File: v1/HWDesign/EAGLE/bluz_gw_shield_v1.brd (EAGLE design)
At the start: 66 x 43.2 mm, 20 parts, among them Q1 FC-12M, U2 MDBT40SMD, U3 SST25VF040B-S2, U4 SPARK_CORE

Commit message: add reset button
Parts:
- added RESET: (no value), Spark:TACTILE_SWITCH_SMD
- moved C1 1.27 mm to (22.8, 40.9)
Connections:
- removed net SWDIO: SWD.2, U2.35
- new net RST: RESET.3, RESET.4, SWD.2, U2.35, U4.#23, U4.23, U4.@23
- net GND: now also RESET.1, RESET.2
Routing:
- net RST: track 0.00 -> 63.0 mm, vias 0 -> 2
- net SWDIO: track 14.9 -> 0.00 mm
- net N$1: track 11.3 -> 10.6 mm
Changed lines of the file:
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@@
 <?xml version="1.0" encoding="utf-8"?>
 <!DOCTYPE eagle SYSTEM "eagle.dtd">
-<eagle version="6.5.0">
+<eagle version="7.3.0">
 <drawing>
 <settings>
@@
 <pass name="Default">
 <param name="RoutingGrid" value="50mil"/>
+<param name="AutoGrid" value="1"/>
+<param name="Efforts" value="0"/>
+<param name="TopRouterVariant" value="1"/>
 <param name="tpViaShape" value="round"/>
 <param name="PrefDir.1" value="|"/>
@@
 <element name="C5" library="SparkFun-Passives" package="0603-CAP" value="12pF" x="10.16" y="3.81" rot="R180"/>
 <element name="C6" library="SparkFun-Passives" package="0603-CAP" value="12pF" x="17.78" y="3.81"/>
-<element name="C1" library="SparkFun-Passives" package="0603-CAP" value="0.1uF" x="24.0538" y="40.8686"/>
+<element name="C1" library="SparkFun-Passives" package="0603-CAP" value="0.1uF" x="22.7838" y="40.8686"/>
 <element name="U1" library="Spark" package="SOT223" value="" x="24.5364" y="35.941" rot="R270"/>
 <element name="JP3" library="SparkFun-Connectors" package="USB-MICROB" value="USB-MICROB" x="14.097" y="40.005" rot="R180">
@@
 <element name="U4" library="Spark" package="SPARK_CORE_STACKABLE" value="SPARK_CORE" x="53.34" y="19.05"/>
 <element name="FRAME1" library="SparkFun-Aesthetics" package="CREATIVE_COMMONS" value="FRAME-LETTER" x="21.59" y="-16.51"/>
+<element name="RESET" library="Spark" package="TACTILE_SWITCH_SMD" value="" x="35.56" y="33.02" smashed="yes">
+<attribute name="NAME" x="34.1884" y="34.7472" size="0.6096" layer="25"/>
+<attribute name="VALUE" x="34.671" y="30.988" size="0.4064" layer="27"/>
+</element>
 </elements>
 <signals>
@@
 <wire x1="15.4732" y1="36.137" x2="18.4912" y2="36.137" width="0.8128" layer="1"/>
 <wire x1="18.4912" y1="36.137" x2="21.4376" y2="38.2524" width="0.8128" layer="1"/>
-<wire x1="23.2038" y1="40.8686" x2="21.5646" y2="39.5732" width="0.8128" layer="1"/>
+<wire x1="21.9338" y1="40.8686" x2="21.5646" y2="39.5732" width="0.8128" layer="1"/>
 <wire x1="21.4376" y1="38.2524" x2="21.4376" y2="39.4462" width="0.8128" layer="1"/>
 <wire x1="21.4376" y1="39.4462" x2="21.5646" y2="39.5732" width="0.8128" layer="1"/>
@@
 <contactref element="U4" pad="@2"/>
 <polygon width="0.254" layer="1">
-<vertex x="5.08" y="2.54"/>
+<vertex x="5.08" y="3.81"/>
 <vertex x="5.08" y="43.18"/>
 <vertex x="66.04" y="43.18"/>
-<vertex x="66.04" y="2.54"/>
+<vertex x="66.04" y="3.81"/>
 </polygon>
 <polygon width="0.254" layer="16">
 <vertex x="66.04" y="43.18"/>
-<vertex x="66.04" y="2.54"/>
-<vertex x="5.08" y="2.54"/>
+<vertex x="66.04" y="3.81"/>
 <vertex x="5.08" y="3.81"/>
 <vertex x="5.08" y="43.18"/>
 </polygon>
-<via x="34.29" y="33.02" extent="1-16" drill="0.6"/>
-<via x="38.1" y="33.02" extent="1-16" drill="0.6"/>
+<via x="31.75" y="31.75" extent="1-16" drill="0.6"/>
+<via x="39.37" y="30.9372" extent="1-16" drill="0.6"/>
 <via x="49.53" y="27.94" extent="1-16" drill="0.6"/>
 <via x="57.15" y="27.94" extent="1-16" drill="0.6"/>
@@
 <via x="8.8138" y="5.2832" extent="1-16" drill="0.381"/>
 <via x="20.3454" y="4.0132" extent="1-16" drill="0.381"/>
+<contactref element="RESET" pad="1"/>
+<contactref element="RESET" pad="2"/>
 </signal>
 <signal name="VCC">
@@
 <wire x1="20.6756" y1="32.3596" x2="20.6756" y2="29.7942" width="0.8128" layer="1"/>
 <wire x1="20.6756" y1="29.7942" x2="21.7424" y2="29.7942" width="0.8128" layer="1"/>
-<wire x1="21.8576" y1="29.7942" x2="21.8576" y2="30.9626" width="0.8128" layer="1"/>
-<wire x1="21.8576" y1="30.9626" x2="21.7424" y2="29.6926" width="0.8128" layer="1"/>
-<wire x1="21.7424" y1="29.6926" x2="21.7424" y2="29.1592" width="0.8128" layer="1"/>
+<wire x1="21.7424" y1="29.7942" x2="21.7424" y2="29.1592" width="0.8128" layer="1"/>
 <wire x1="21.7424" y1="29.1592" x2="20.701" y2="29.21" width="0.8128" layer="1"/>
 <wire x1="21.8576" y1="29.7942" x2="21.7424" y2="29.7942" width="0.8128" layer="1"/>
-<wire x1="21.7424" y1="29.7942" x2="21.7424" y2="29.6926" width="0.8128" layer="1"/>
 <wire x1="21.7424" y1="29.1592" x2="24.4602" y2="29.21" width="0.8128" layer="1"/>
 <wire x1="24.4602" y1="29.21" x2="34.2646" y2="36.6268" width="0.8128" layer="1"/>
@@
 <wire x1="59.69" y1="33.02" x2="62.23" y2="33.02" width="0.8128" layer="1"/>
 <wire x1="64.77" y1="33.02" x2="62.23" y2="33.02" width="0.8128" layer="1"/>
+<wire x1="21.8576" y1="30.9626" x2="21.8576" y2="32.7524" width="0.8128" layer="1"/>
+<wire x1="21.8576" y1="32.7524" x2="21.59" y2="33.02" width="0.8128" layer="1"/>
+<wire x1="21.59" y1="33.02" x2="21.59" y2="33.4772" width="0.8128" layer="1"/>
+<wire x1="21.59" y1="33.4772" x2="21.4376" y2="33.6296" width="0.8128" layer="1"/>
 </signal>
 <signal name="N$5">
@@
 <wire x1="12.7" y1="23.4188" x2="17.5768" y2="23.4188" width="0.3048" layer="1"/>
 <wire x1="17.5768" y1="23.4188" x2="17.5768" y2="25.244" width="0.3048" layer="1"/>
-</signal>
-<signal name="SWDIO">
-<contactref element="U2" pad="35"/>
-<contactref element="SWD" pad="2"/>
-<wire x1="9.79" y1="16.43" x2="9.79" y2="18.1466" width="0.3048" layer="1"/>
-<wire x1="9.79" y1="18.1466" x2="13.0556" y2="22.6822" width="0.3048" layer="1"/>
-<wire x1="13.0556" y1="22.6822" x2="17.5768" y2="22.6822" width="0.3048" layer="1"/>
-<wire x1="17.5768" y1="22.6822" x2="18.7706" y2="23.876" width="0.3048" layer="1"/>
-<wire x1="18.7706" y1="23.876" x2="18.7706" y2="25.1678" width="0.3048" layer="1"/>
-<wire x1="18.7706" y1="25.1678" x2="18.8468" y2="25.244" width="0.3048" layer="1"/>
 </signal>
 <signal name="SS">
@@
 <wire x1="44.45" y1="27.94" x2="46.99" y2="27.94" width="0.3048" layer="1"/>
 </signal>
+<signal name="RST">
+<contactref element="U2" pad="35"/>
+<contactref element="SWD" pad="2"/>
+<wire x1="9.79" y1="18.1466" x2="13.0556" y2="22.6822" width="0.3048" layer="1"/>
+<wire x1="13.0556" y1="22.6822" x2="17.5768" y2="22.6822" width="0.3048" layer="1"/>
+<wire x1="17.5768" y1="22.6822" x2="18.7706" y2="23.876" width="0.3048" layer="1"/>
+<wire x1="18.7706" y1="23.876" x2="18.7706" y2="25.1678" width="0.3048" layer="1"/>
+<wire x1="18.7706" y1="25.1678" x2="18.8468" y2="25.244" width="0.3048" layer="1"/>
+<contactref element="U4" pad="23"/>
+<contactref element="U4" pad="#23"/>
+<contactref element="U4" pad="@23"/>
+<contactref element="RESET" pad="3"/>
+<contactref element="RESET" pad="4"/>
+<wire x1="37.435" y1="32.245" x2="39.37" y2="32.245" width="0.4064" layer="1"/>
+<wire x1="39.37" y1="32.245" x2="39.37" y2="35.56" width="0.4064" layer="1"/>
+<wire x1="39.37" y1="35.56" x2="54.61" y2="35.56" width="0.4064" layer="1"/>
+<wire x1="54.61" y1="35.56" x2="59.69" y2="30.48" width="0.4064" layer="1"/>
+<wire x1="18.8468" y1="25.244" x2="20.5958" y2="25.244" width="0.4064" layer="1"/>
+<wire x1="20.5958" y1="25.244" x2="22.5552" y2="27.2034" width="0.4064" layer="1"/>
+<via x="22.5552" y="27.2034" extent="1-16" drill="0.635"/>
+<wire x1="22.5552" y1="27.2034" x2="29.7688" y2="27.2034" width="0.4064" layer="16"/>
+<wire x1="29.7688" y1="27.2034" x2="33.528" y2="30.9626" width="0.4064" layer="16"/>
+<via x="33.528" y="30.9626" extent="1-16" drill="0.635"/>
+<wire x1="33.528" y1="30.9626" x2="33.528" y2="32.088" width="0.4064" layer="1"/>
+<wire x1="33.528" y1="32.088" x2="33.685" y2="32.245" width="0.4064" layer="1"/>
+<wire x1="33.685" y1="32.245" x2="37.435" y2="32.245" width="0.4064" layer="1"/>
+<wire x1="62.23" y1="30.48" x2="64.77" y2="30.48" width="0" layer="19" extent="1-1"/>
+<wire x1="59.69" y1="30.48" x2="62.23" y2="30.48" width="0" layer="19" extent="1-1"/>
+<wire x1="9.79" y1="16.43" x2="9.79" y2="18.1466" width="0" layer="19" extent="1-1"/>
+</signal>
 </signals>

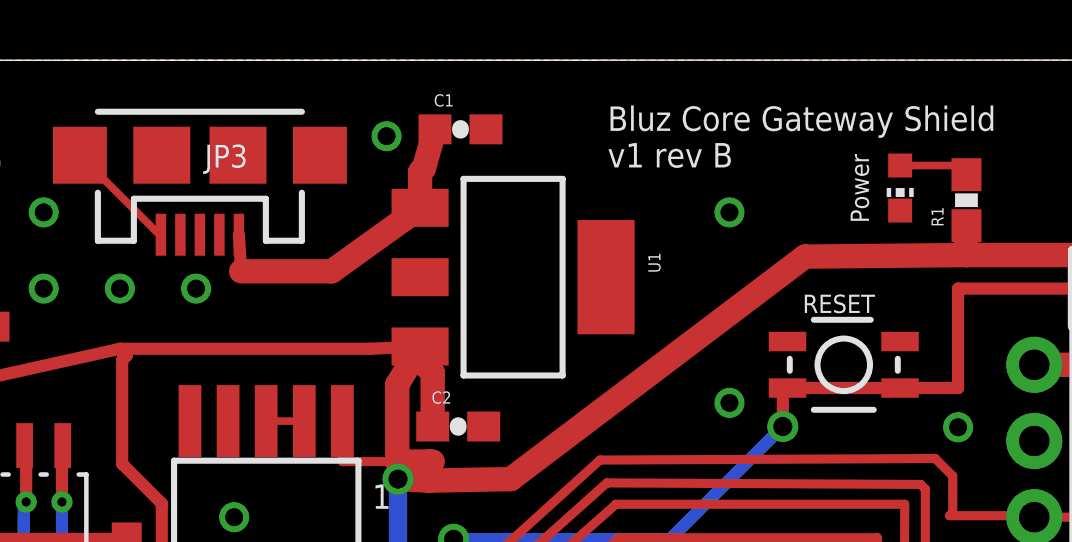
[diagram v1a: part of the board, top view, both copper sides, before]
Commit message: updated BOM, was missing a few things
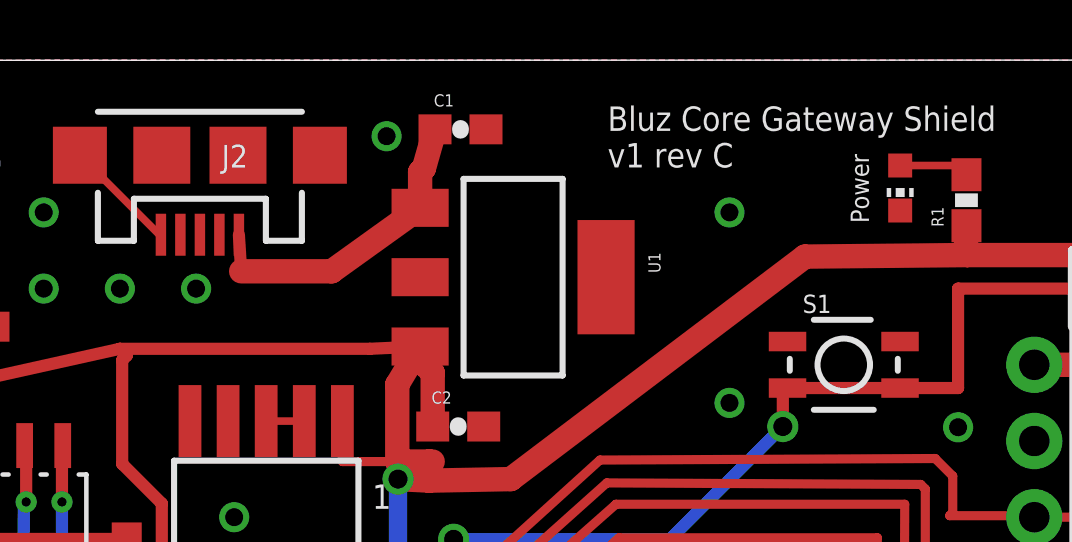
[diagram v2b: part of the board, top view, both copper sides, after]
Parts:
- renumbered JP3 to J2, RESET to S1
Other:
- board text added: "Bluz Core Gateway Shield v1 rev C"
- board text removed: "Bluz Core Gateway Shield v1 rev B"
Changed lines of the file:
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@@
 <text x="19.8374" y="28.2194" size="0.8128" layer="25" rot="SR0">1</text>
 <text x="27.686" y="39.5986" size="0.8128" layer="25">Bluz Core Gateway Shield
-v1 rev B</text>
+v1 rev C</text>
 <text x="33.528" y="4.826" size="0.6096" layer="21">D0</text>
 <text x="33.528" y="7.366" size="0.6096" layer="21">D1</text>
@@
 <element name="C1" library="SparkFun-Passives" package="0603-CAP" value="0.1uF" x="22.7838" y="40.8686"/>
 <element name="U1" library="Spark" package="SOT223" value="" x="24.5364" y="35.941" rot="R270"/>
-<element name="JP3" library="SparkFun-Connectors" package="USB-MICROB" value="USB-MICROB" x="14.097" y="40.005" rot="R180">
+<element name="J2" library="SparkFun-Connectors" package="USB-MICROB" value="USB-MICROB" x="14.097" y="40.005" rot="R180">
 <attribute name="PROD_ID" value="CONN-09505" x="-4.953" y="81.915" size="1.778" layer="27" rot="R180" display="off"/>
 </element>
@@
 <element name="U4" library="Spark" package="SPARK_CORE_STACKABLE" value="SPARK_CORE" x="53.34" y="19.05"/>
 <element name="FRAME1" library="SparkFun-Aesthetics" package="CREATIVE_COMMONS" value="FRAME-LETTER" x="21.59" y="-16.51"/>
-<element name="RESET" library="Spark" package="TACTILE_SWITCH_SMD" value="" x="35.56" y="33.02" smashed="yes">
+<element name="S1" library="Spark" package="TACTILE_SWITCH_SMD" value="" x="35.56" y="33.02" smashed="yes">
 <attribute name="NAME" x="34.1884" y="34.7472" size="0.6096" layer="25"/>
 <attribute name="VALUE" x="34.671" y="30.988" size="0.4064" layer="27"/>
@@
 <signals>
 <signal name="N$1">
-<contactref element="JP3" pad="VBUS"/>
+<contactref element="J2" pad="VBUS"/>
 <contactref element="U1" pad="1"/>
 <contactref element="C1" pad="1"/>
@@
 <wire x1="4.89" y1="6.43" x2="5.59" y2="6.43" width="0.254" layer="1"/>
 <wire x1="4.89" y1="16.43" x2="4.89" y2="6.43" width="0.254" layer="1"/>
-<contactref element="JP3" pad="GND"/>
-<contactref element="JP3" pad="MT2"/>
-<contactref element="JP3" pad="MT1"/>
+<contactref element="J2" pad="GND"/>
+<contactref element="J2" pad="MT2"/>
+<contactref element="J2" pad="MT1"/>
 <wire x1="17.760084375" y1="40.19090625" x2="17.97" y2="40.196" width="0.254" layer="1"/>
 <wire x1="17.97" y1="40.196" x2="17.399" y2="40.767" width="0.254" layer="1"/>
@@
 <via x="8.8138" y="5.2832" extent="1-16" drill="0.381"/>
 <via x="20.3454" y="4.0132" extent="1-16" drill="0.381"/>
-<contactref element="RESET" pad="1"/>
-<contactref element="RESET" pad="2"/>
+<contactref element="S1" pad="1"/>
+<contactref element="S1" pad="2"/>
 </signal>
 <signal name="VCC">
@@
 <contactref element="U4" pad="#23"/>
 <contactref element="U4" pad="@23"/>
-<contactref element="RESET" pad="3"/>
-<contactref element="RESET" pad="4"/>
+<contactref element="S1" pad="3"/>
+<contactref element="S1" pad="4"/>
 <wire x1="37.435" y1="32.245" x2="39.37" y2="32.245" width="0.4064" layer="1"/>
 <wire x1="39.37" y1="32.245" x2="39.37" y2="35.56" width="0.4064" layer="1"/>
